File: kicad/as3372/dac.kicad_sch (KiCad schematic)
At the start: 28 parts, among them U13 LM4040AIM3-2.5, U4 TL074, U9 AD5328

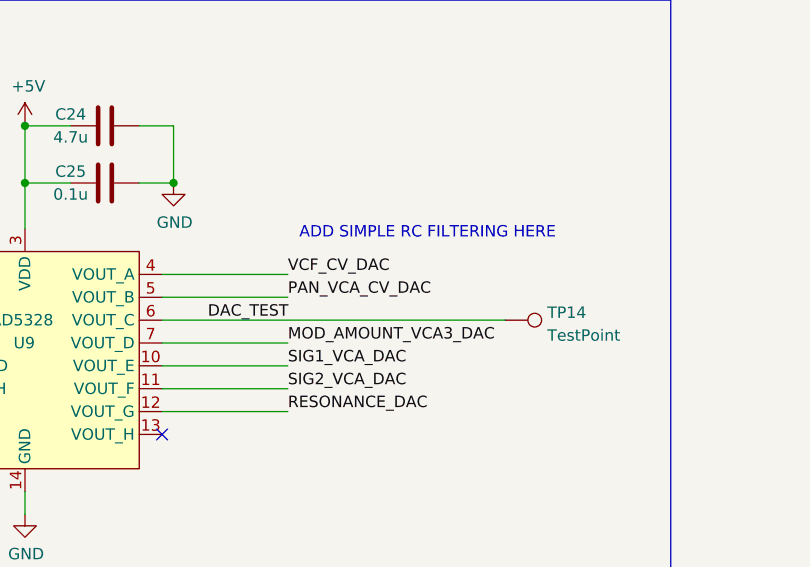
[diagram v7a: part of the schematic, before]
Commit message: add white noise enable/powerdown
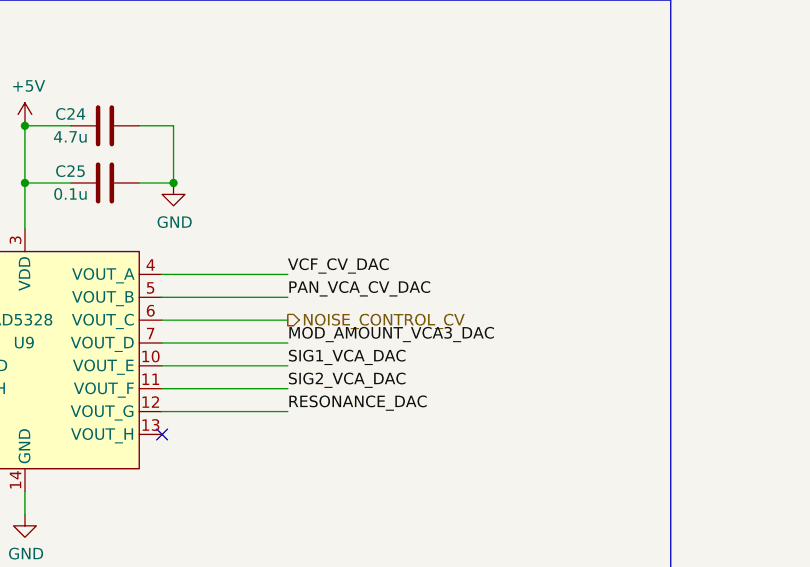
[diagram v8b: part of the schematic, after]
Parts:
- removed TP14: TestPoint, TestPoint:TestPoint_Pad_2.0x2.0mm, symbol Connector:TestPoint
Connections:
- net DAC_TEST renamed NOISE_CONTROL_CV
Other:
- note removed: "ADD SIMPLE RC FILTERING HERE"
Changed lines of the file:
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@@
-    (stroke (width 0) (type default) (color 0 0 0 0))
-  )
-  (wire (pts (xy 91.44 54.61) (xy 129.54 54.61))
     (stroke (width 0) (type default) (color 0 0 0 0))
   )
@@
   )
   (wire (pts (xy 245.745 114.3) (xy 247.015 114.3))
+    (stroke (width 0) (type default) (color 0 0 0 0))
+  )
+  (wire (pts (xy 91.44 54.61) (xy 105.41 54.61))
     (stroke (width 0) (type default) (color 0 0 0 0))
   )
@@
     (effects (font (size 1.27 1.27)) (justify left bottom))
   )
-  (text "ADD SIMPLE RC FILTERING HERE" (at 106.68 45.72 0)
-    (effects (font (size 1.27 1.27)) (justify left bottom))
-  )
   (text "Control Voltage levels:\nSig1 VCA CV: 0-5V\nSig2 VCA CV: 0-5V\nVCA Mod Level CV: 0-5V\nRes CV: 0-5V\nVCF CV: -1 - +6V\nPan VCA CV: -2.5  - +2.5V\n\nThe latter two use opamps to scale; everything else can be\nstraight from DAC.  These are slightly outside datasheet specs\nof 0:5 and -2:+2 to allow for some offset from modulation."
     (at 34.925 121.92 0)
@@
     (effects (font (size 1.27 1.27)) (justify left bottom))
   )
-  (label "DAC_TEST" (at 96.52 54.61 0)
-    (effects (font (size 1.27 1.27)) (justify left bottom))
-  )
   (label "VREF_2.5V_BUFFERED" (at 236.855 64.77 180)
     (effects (font (size 1.27 1.27)) (justify right bottom))
@@
   )
   (hierarchical_label "VCF_CV" (shape output) (at 277.495 67.31 0)
+    (effects (font (size 1.27 1.27)) (justify left))
+  )
+  (hierarchical_label "NOISE_CONTROL_CV" (shape output) (at 105.41 54.61 0)
     (effects (font (size 1.27 1.27)) (justify left))
   )
@@
     (pin "2")
   )
-  (symbol (lib_id "Connector:TestPoint") (at 129.54 54.61 270) (unit 1)
-    (in_bom yes) (on_board yes) (fields_autoplaced)
-    (property "Reference" "TP14" (id 0) (at 134.239 53.7753 90)
-      (effects (font (size 1.27 1.27)) (justify left))
-    )
-    (property "Value" "TestPoint" (id 1) (at 134.239 56.3122 90)
-      (effects (font (size 1.27 1.27)) (justify left))
-    )
-    (property "Footprint" "TestPoint:TestPoint_Pad_2.0x2.0mm" (id 2) (at 129.54 59.69 0)
-      (effects (font (size 1.27 1.27)) hide)
-    )
-    (property "Datasheet" "~" (id 3) (at 129.54 59.69 0)
-      (effects (font (size 1.27 1.27)) hide)
-    )
-    (pin "1")
-  )
   (symbol (lib_id "Device:R") (at 241.935 69.85 90) (unit 1)
